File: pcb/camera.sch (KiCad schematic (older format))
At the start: 0 parts

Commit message: MCU change, again
STM32L0 had quite a big problem, common reference for the comparators.
Another minus was the missing SWO for debugging.

STM32L4 has floating point, and most importantly, has embedded OPAMPS!
This means I can directly plug in the filter to the analog inputs and
everything is software. 2 opamps and 2 comparators (if needed).
External circuitry would be minimal for the PIR sensor.

It also means that I can read with the embedded 12-bit ADC the
amplified values. Precision is not crucial, we are interested in dips
and swells.
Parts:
- added IC? (x2): SI2302CDS, SOT95P237X112-3N, symbol SI2302CDS-T1-GE3:SI2302CDS-T1-GE3
- added J?: AUDIO-JACK2.5MM, SparkFun-STEREOJACK2.5MM_STEREOJACK2.5MM, symbol AUDIO-JACK2.5MM
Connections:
- net labels added: RING, SHIELD, TIP
- wire segments 0 -> 17
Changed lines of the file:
@@
 EESchema Schematic File Version 2
+LIBS:74xgxx
+LIBS:74xx
+LIBS:Altera
+LIBS:ESD_Protection
+LIBS:LEM
+LIBS:Lattice
+LIBS:Oscillators
+LIBS:Power_Management
+LIBS:RFSolutions
+LIBS:Worldsemi
+LIBS:Xicor
+LIBS:Zilog
+LIBS:ac-dc
+LIBS:actel
+LIBS:adc-dac
+LIBS:allegro
+LIBS:analog_devices
+LIBS:analog_switches
+LIBS:atmel
+LIBS:audio
+LIBS:battery_management
+LIBS:bbd
+LIBS:bosch
+LIBS:brooktre
+LIBS:cmos4000
+LIBS:cmos_ieee
+LIBS:conn
+LIBS:contrib
+LIBS:cypress
+LIBS:dc-dc
+LIBS:device
+LIBS:digital-audio
+LIBS:diode
+LIBS:display
+LIBS:dsp
+LIBS:elec-unifil
+LIBS:ftdi
+LIBS:gennum
+LIBS:graphic_symbols
+LIBS:hc11
+LIBS:infineon
+LIBS:intel
+LIBS:interface
+LIBS:intersil
+LIBS:ir
+LIBS:leds
+LIBS:linear
+LIBS:logic_programmable
+LIBS:maxim
+LIBS:mechanical
+LIBS:memory
+LIBS:microchip
+LIBS:microchip_dspic33dsc
+LIBS:microchip_pic10mcu
+LIBS:microchip_pic12mcu
+LIBS:microchip_pic16mcu
+LIBS:microchip_pic18mcu
+LIBS:microchip_pic24mcu
+LIBS:microchip_pic32mcu
+LIBS:microcontrollers
+LIBS:modules
+LIBS:motor_drivers
+LIBS:motorola
+LIBS:motors
+LIBS:msp430
+LIBS:nordicsemi
+LIBS:nxp
+LIBS:nxp_armmcu
+LIBS:onsemi
+LIBS:opto
+LIBS:philips
 LIBS:power
+LIBS:powerint
+LIBS:pspice
+LIBS:references
+LIBS:regul
+LIBS:relays
+LIBS:rfcom
+LIBS:sensors
+LIBS:silabs
+LIBS:siliconi
+LIBS:stm32
+LIBS:stm8
+LIBS:supertex
+LIBS:switches
+LIBS:texas
+LIBS:transf
+LIBS:transistors
+LIBS:triac_thyristor
+LIBS:ttl_ieee
+LIBS:valves
+LIBS:video
+LIBS:wiznet
+LIBS:xilinx
+LIBS:zetex
+LIBS:SparkFun
+LIBS:ab2_7segment
+LIBS:ab2_audio
+LIBS:ab2_buffer
+LIBS:ab2_capacitor
+LIBS:ab2_connectivity
+LIBS:ab2_dac
+LIBS:ab2_diode
+LIBS:ab2_fuse
+LIBS:ab2_gpio_expansion
+LIBS:ab2_header
+LIBS:ab2_idc
+LIBS:ab2_inductor
+LIBS:ab2_input_devices
+LIBS:ab2_jumper
+LIBS:ab2_lcd
+LIBS:ab2_led
+LIBS:ab2_memory
+LIBS:ab2_opamp
+LIBS:ab2_pinouts
+LIBS:ab2_pot
+LIBS:ab2_power
+LIBS:ab2_regulator
+LIBS:ab2_relay
+LIBS:ab2_resistor
+LIBS:ab2_sensor
+LIBS:ab2_stepper
+LIBS:ab2_supply
+LIBS:ab2_terminal_block
+LIBS:ab2_test
+LIBS:ab2_transistor
+LIBS:ab2_uC
+LIBS:ab2_usb
+LIBS:ab2_xtal
 LIBS:pir-cache
 EELAYER 25 0
@@
 Comment4 ""
 $EndDescr
-Text HLabel 2350 2700 0    60   Input ~ 0
+Text HLabel 5300 2050 0    60   Input ~ 0
 FOCUS
-Text HLabel 2400 3300 0    60   Input ~ 0
+Text HLabel 5250 3250 0    60   Input ~ 0
 SHUTTER
+$Comp
+L AUDIO-JACK2.5MM J?
+U 1 1 5A8040DB
+P 1900 2500
+F 0 "J?" H 1700 2620 50  0000 L BNN
+F 1 "AUDIO-JACK2.5MM" H 1700 2300 50  0000 L BNN
+F 2 "SparkFun-STEREOJACK2.5MM_STEREOJACK2.5MM" H 2000 2250 50  0001 C CNN
+F 3 "" H 1900 2500 60  0001 C CNN
+	1    1900 2500
+	1    0    0    -1
+$EndComp
+$Comp
+L SI2302CDS-T1-GE3:SI2302CDS-T1-GE3 IC?
+U 1 1 5A804D7D
+P 5600 2050
+F 0 "IC?" H 6250 2350 50  0000 L CNN
+F 1 "SI2302CDS" H 6250 2250 50  0000 L CNN
+F 2 "SOT95P237X112-3N" H 6250 2150 50  0001 L CNN
+F 3 "http://www.vishay.com/docs/68645/si2302cd.pdf" H 6250 2050 50  0001 L CNN
+F 4 "SI2302CDS-T1-GE3, N-channel MOSFET Transistor 2.6 A 20 V, 3-Pin SOT-23" H 6250 1950 50  0001 L CNN "Description"
+F 5 "Vishay" H 6250 1850 50  0001 L CNN "Manufacturer_Name"
+F 6 "SI2302CDS-T1-GE3" H 6250 1750 50  0001 L CNN "Manufacturer_Part_Number"
+F 7 "RS" H 6250 1650 50  0001 L CNN "Supplier_Name"
+F 8 "7103232P" H 6250 1550 50  0001 L CNN "RS Part Number"
+F 9 "1.12" H 6250 1450 50  0001 L CNN "Height"
+	1    5600 2050
+	1    0    0    -1
+$EndComp
+Text GLabel 2550 2600 2    60   Input ~ 0
+SHIELD
+Text GLabel 2550 2450 2    60   Input ~ 0
+RING
+Text GLabel 2550 2300 2    60   Input ~ 0
+TIP
+Wire Wire Line
+	2100 2600 2550 2600
+Wire Wire Line
+	2100 2500 2350 2500
+Wire Wire Line
+	2350 2500 2350 2450
+Wire Wire Line
+	2350 2450 2550 2450
+Wire Wire Line
+	2100 2400 2350 2400
+Wire Wire Line
+	2350 2400 2350 2300
+Wire Wire Line
+	2350 2300 2550 2300
+Wire Wire Line
+	5300 2050 5600 2050
+Text GLabel 6800 2050 2    60   Input ~ 0
+RING
+Wire Wire Line
+	6400 2050 6800 2050
+Text GLabel 6800 2350 2    60   Input ~ 0
+SHIELD
+Wire Wire Line
+	5600 2150 5500 2150
+Wire Wire Line
+	5500 2150 5500 2350
+Wire Wire Line
+	5500 2350 6800 2350
+$Comp
+L SI2302CDS-T1-GE3:SI2302CDS-T1-GE3 IC?
+U 1 1 5A805147
+P 5550 3250
+F 0 "IC?" H 6200 3550 50  0000 L CNN
+F 1 "SI2302CDS" H 6200 3450 50  0000 L CNN
+F 2 "SOT95P237X112-3N" H 6200 3350 50  0001 L CNN
+F 3 "http://www.vishay.com/docs/68645/si2302cd.pdf" H 6200 3250 50  0001 L CNN
+F 4 "SI2302CDS-T1-GE3, N-channel MOSFET Transistor 2.6 A 20 V, 3-Pin SOT-23" H 6200 3150 50  0001 L CNN "Description"
+F 5 "Vishay" H 6200 3050 50  0001 L CNN "Manufacturer_Name"
+F 6 "SI2302CDS-T1-GE3" H 6200 2950 50  0001 L CNN "Manufacturer_Part_Number"
+F 7 "RS" H 6200 2850 50  0001 L CNN "Supplier_Name"
+F 8 "7103232P" H 6200 2750 50  0001 L CNN "RS Part Number"
+F 9 "1.12" H 6200 2650 50  0001 L CNN "Height"
+	1    5550 3250
+	1    0    0    -1
+$EndComp
+Wire Wire Line
+	5250 3250 5550 3250
+Text GLabel 6750 3250 2    60   Input ~ 0
+TIP
+Wire Wire Line
+	6350 3250 6750 3250
+Text GLabel 6750 3550 2    60   Input ~ 0
+SHIELD
+Wire Wire Line
+	5550 3350 5450 3350
+Wire Wire Line
+	5450 3350 5450 3550
+Wire Wire Line
+	5450 3550 6750 3550
 $EndSCHEMATC

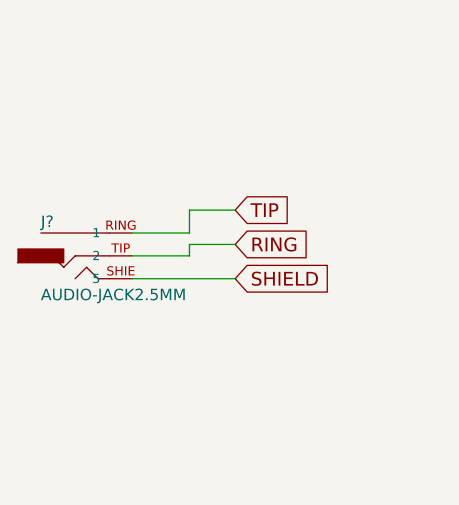
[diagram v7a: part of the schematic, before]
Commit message: Renamed all components
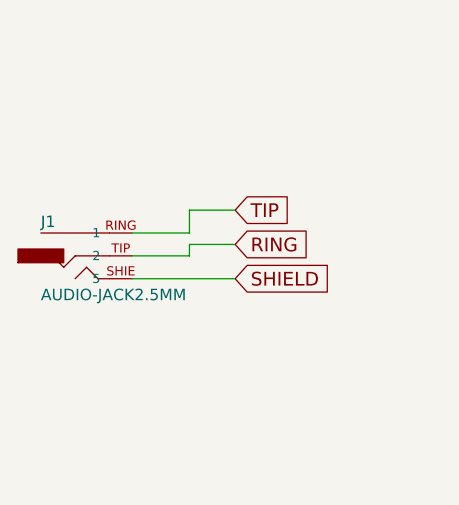
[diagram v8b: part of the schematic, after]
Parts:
- gave numbers to parts that had none: 3
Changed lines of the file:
@@
 LIBS:ab2_usb
 LIBS:ab2_xtal
+LIBS:pir-cache
 EELAYER 25 0
 EELAYER END
@@
 SHUTTER
 $Comp
-L AUDIO-JACK2.5MM J?
+L AUDIO-JACK2.5MM J1
 U 1 1 5A8040DB
 P 1900 2500
-F 0 "J?" H 1700 2620 50  0000 L BNN
+F 0 "J1" H 1700 2620 50  0000 L BNN
 F 1 "AUDIO-JACK2.5MM" H 1700 2300 50  0000 L BNN
 F 2 "SparkFun-STEREOJACK2.5MM_STEREOJACK2.5MM" H 2000 2250 50  0001 C CNN
@@
 $EndComp
 $Comp
-L SI2302CDS-T1-GE3:SI2302CDS-T1-GE3 IC?
+L SI2302CDS-T1-GE3:SI2302CDS-T1-GE3 IC4
 U 1 1 5A804D7D
 P 5600 2050
-F 0 "IC?" H 6250 2350 50  0000 L CNN
+F 0 "IC4" H 6250 2350 50  0000 L CNN
 F 1 "SI2302CDS" H 6250 2250 50  0000 L CNN
 F 2 "SOT95P237X112-3N" H 6250 2150 50  0001 L CNN
@@
 	5500 2350 6800 2350
 $Comp
-L SI2302CDS-T1-GE3:SI2302CDS-T1-GE3 IC?
+L SI2302CDS-T1-GE3:SI2302CDS-T1-GE3 IC3
 U 1 1 5A805147
 P 5550 3250
-F 0 "IC?" H 6200 3550 50  0000 L CNN
+F 0 "IC3" H 6200 3550 50  0000 L CNN
 F 1 "SI2302CDS" H 6200 3450 50  0000 L CNN
 F 2 "SOT95P237X112-3N" H 6200 3350 50  0001 L CNN
